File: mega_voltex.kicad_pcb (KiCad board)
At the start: 2 copper layers, 10 parts, among them J1 Arduino_Mega_Header

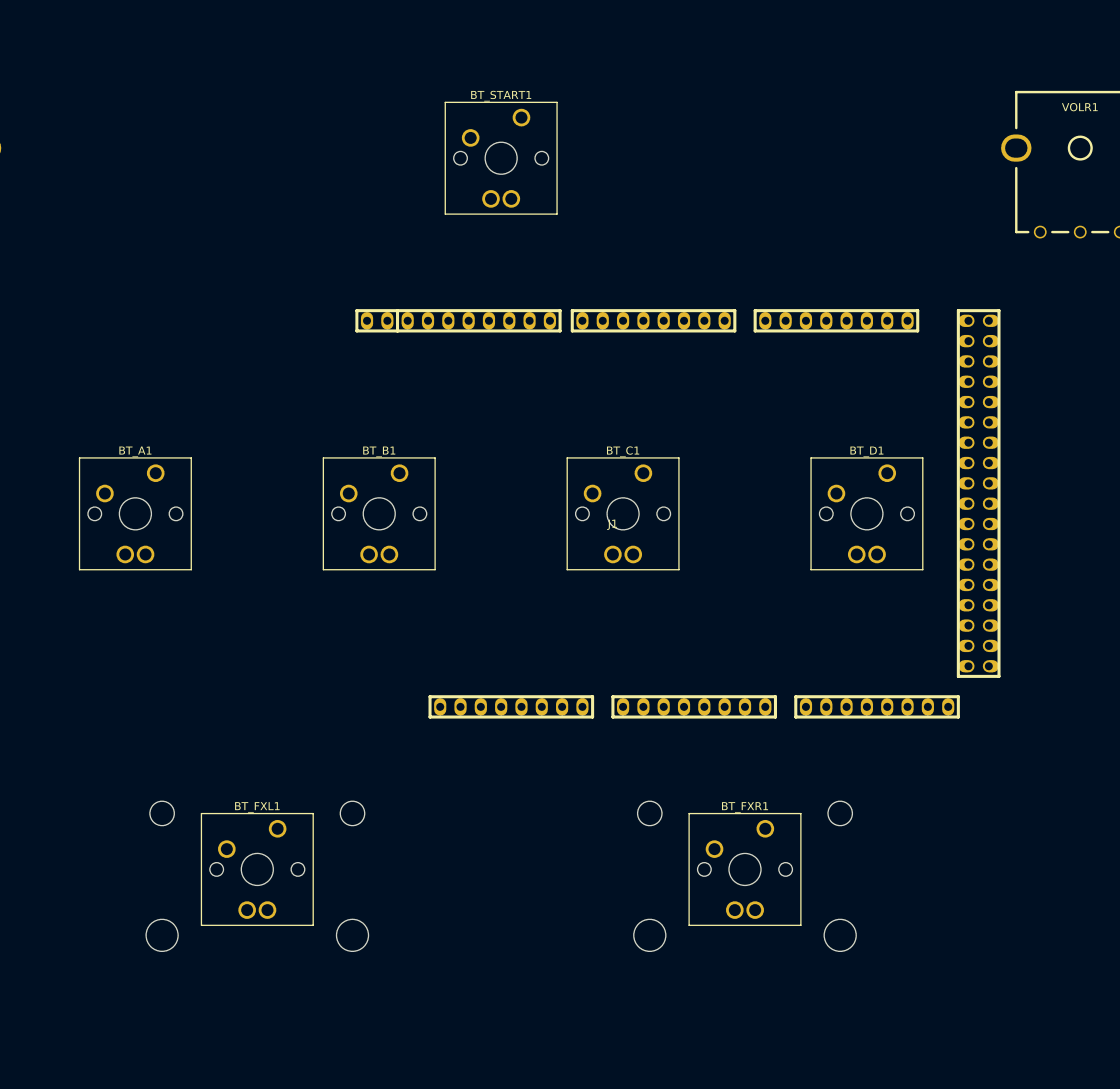
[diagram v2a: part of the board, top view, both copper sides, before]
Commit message: Added headers & resistors for LEDs
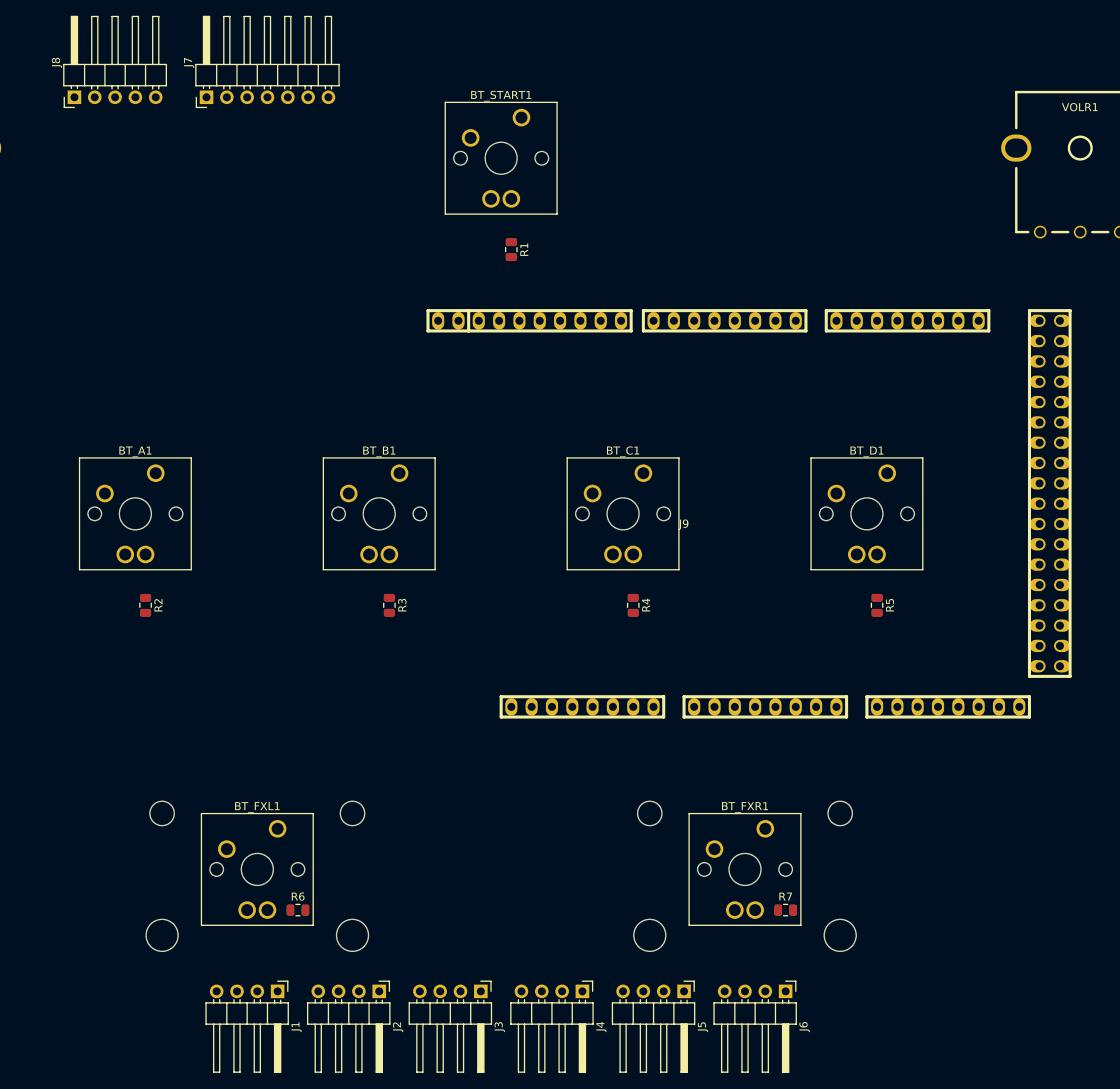
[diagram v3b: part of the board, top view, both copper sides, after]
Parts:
- added J2: HEADER_4, Connector_PinHeader_2.54mm:PinHeader_1x04_P2.54mm_Horizontal, F.Cu at (116.8, 142.2)
- added J3: HEADER_4, Connector_PinHeader_2.54mm:PinHeader_1x04_P2.54mm_Horizontal, F.Cu at (129.5, 142.2)
- added J4: HEADER_4, Connector_PinHeader_2.54mm:PinHeader_1x04_P2.54mm_Horizontal, F.Cu at (142.2, 142.2)
- added J5: HEADER_4, Connector_PinHeader_2.54mm:PinHeader_1x04_P2.54mm_Horizontal, F.Cu at (154.9, 142.2)
- added J6: HEADER_4, Connector_PinHeader_2.54mm:PinHeader_1x04_P2.54mm_Horizontal, F.Cu at (167.6, 142.2)
- added J7: HEADER_7, Connector_PinHeader_2.54mm:PinHeader_1x07_P2.54mm_Horizontal, F.Cu at (95.2, 30.5)
- added J8: HEADER_5, Connector_PinHeader_2.54mm:PinHeader_1x05_P2.54mm_Horizontal, F.Cu at (78.7, 30.5)
- added J9: Arduino_Mega_Header, mega_voltex:arduino_mega_header, F.Cu at (154.9, 82.5)
- added R1: R_Small_US, Resistor_SMD:R_0805_2012Metric, F.Cu at (133.3, 49.5)
- added R2: R_Small_US, Resistor_SMD:R_0805_2012Metric, F.Cu at (87.6, 94.0)
- added R3: R_Small_US, Resistor_SMD:R_0805_2012Metric, F.Cu at (118.1, 94.0)
- added R4: R_Small_US, Resistor_SMD:R_0805_2012Metric, F.Cu at (148.6, 94.0)
- added R5: R_Small_US, Resistor_SMD:R_0805_2012Metric, F.Cu at (179.1, 94.0)
- added R6: R_Small_US, Resistor_SMD:R_0805_2012Metric, F.Cu at (106.7, 132.1)
- added R7: R_Small_US, Resistor_SMD:R_0805_2012Metric, F.Cu at (167.6, 132.1)
- J1: value Arduino_Mega_Header -> HEADER_4; footprint mega_voltex:arduino_mega_header -> Connector_PinHeader_2.54mm:PinHeader_1x04_P2.54mm_Horizontal
- moved J1 72.9 mm to (104.1, 142.2), turned to 270 degrees
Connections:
- BT_A1 pad 4: LT_A -> Net-(BT_A1-Pad4)
- BT_B1 pad 4: LT_B -> Net-(BT_B1-Pad4)
- BT_C1 pad 4: LT_C -> Net-(BT_C1-Pad4)
- BT_D1 pad 4: LT_D -> Net-(BT_D1-Pad4)
- BT_FXL1 pad 4: LT_FXL -> Net-(BT_FXL1-Pad4)
- BT_FXR1 pad 4: LT_FXR -> Net-(BT_FXR1-Pad4)
- BT_START1 pad 4: LT_START -> Net-(BT_START1-Pad4)
- J1 pad 1: (no net) -> GND
- J1 pad 2: Net-(J1-Pad2) -> LED1_R
- J1 pad 3: Net-(J1-Pad3) -> LED1_G
- J1 pad 4: Net-(J1-Pad4) -> LED1_B
- VOLL1 pad A: Net-(VOLL1-PadA) -> VOLL_A
- VOLL1 pad C: Net-(VOLL1-PadC) -> VOLL_B
- VOLR1 pad A: Net-(VOLR1-PadA) -> VOLR_A
- VOLR1 pad C: Net-(VOLR1-PadC) -> VOLR_B

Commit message: Lots of changes. PCB without LED1-5 headers is nearly complete
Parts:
- removed J1, J2, J3, J4, J5, J6: HEADER_4, Connector_PinHeader_2.54mm:PinHeader_1x04_P2.54mm_Horizontal
- added D1: LED_RGB, LED_SMD:LED_RGB_Cree-PLCC-6_6x5mm_P2.1mm, F.Cu at (57.5, 25.0)
- added D2: LED_RGB, LED_SMD:LED_RGB_Cree-PLCC-6_6x5mm_P2.1mm, F.Cu at (122.5, 25.0)
- added D3: LED_RGB, LED_SMD:LED_RGB_Cree-PLCC-6_6x5mm_P2.1mm, F.Cu at (20.0, 85.0)
- added D4: LED_RGB, LED_SMD:LED_RGB_Cree-PLCC-6_6x5mm_P2.1mm, F.Cu at (160.0, 85.0)
- added Q1: PN2222A, Package_TO_SOT_SMD:SOT-323_SC-70, F.Cu at (154.5, 91.5)
- added Q2: PN2222A, Package_TO_SOT_SMD:SOT-323_SC-70, F.Cu at (154.5, 96.0)
- added Q3: PN2222A, Package_TO_SOT_SMD:SOT-323_SC-70, F.Cu at (154.5, 100.5)
- added R10: R_Small_US, Resistor_SMD:R_0805_2012Metric, F.Cu at (70.0, 28.5)
- added R11: R_Small_US, Resistor_SMD:R_0805_2012Metric, F.Cu at (135.0, 21.2)
- added R12: R_Small_US, Resistor_SMD:R_0805_2012Metric, F.Cu at (135.0, 25.0)
- added R13: R_Small_US, Resistor_SMD:R_0805_2012Metric, F.Cu at (135.0, 28.8)
- added R14: R_Small_US, Resistor_SMD:R_0805_2012Metric, F.Cu at (16.5, 75.0)
- added R15: R_Small_US, Resistor_SMD:R_0805_2012Metric, F.Cu at (20.0, 75.0)
- added R16: R_Small_US, Resistor_SMD:R_0805_2012Metric, F.Cu at (23.5, 75.0)
- added R17: R_Small_US, Resistor_SMD:R_0805_2012Metric, F.Cu at (156.5, 75.0)
- added R18: R_Small_US, Resistor_SMD:R_0805_2012Metric, F.Cu at (160.0, 75.0)
- added R19: R_Small_US, Resistor_SMD:R_0805_2012Metric, F.Cu at (163.5, 75.0)
- added R8: R_Small_US, Resistor_SMD:R_0805_2012Metric, F.Cu at (70.0, 21.5)
- added R9: R_Small_US, Resistor_SMD:R_0805_2012Metric, F.Cu at (70.0, 25.0)
- J7, J8, R1, R2, R3, R4, R5, R6, R7: moved to B.Cu
- moved J7 69.6 mm to (159.0, 58.5), turned to 0 degrees
- moved J9 52.9 mm to (105.0, 65.0)
- moved VOLR1 50.9 mm to (155.0, 25.0)
- moved BT_FXR1 48.2 mm to (120.0, 105.0)
- moved R7 48.0 mm to (125.1, 110.0)
- moved BT_FXL1 47.3 mm to (60.0, 105.0)
- moved R6 47.2 mm to (65.0, 110.0)
- moved BT_D1 47.0 mm to (135.0, 65.0)
- moved BT_C1 46.6 mm to (105.0, 65.0)
- moved BT_B1 46.1 mm to (75.0, 65.0)
- moved R5 45.8 mm to (140.0, 70.0), turned to 0 degrees
- moved BT_A1 45.6 mm to (45.0, 65.0)
- moved R4 45.4 mm to (110.1, 70.0), turned to 0 degrees
- moved BT_START1 45.3 mm to (90.0, 25.0)
- moved R3 45.0 mm to (80.1, 70.0), turned to 0 degrees
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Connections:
- J7 pad 1: K1_A -> K1_4
- J7 pad 2: K1_B -> K1_3
- J7 pad 3: K1_C -> K1_2
- J7 pad 5: K1_2 -> K1_C
- J7 pad 6: K1_3 -> K1_B
- J7 pad 7: K1_4 -> K1_A
- J8 pad 3: R1_TX -> R1_DET
- J8 pad 5: R1_DET -> R1_TX
- J9 pad 17: LED6_R -> Net-(J9-Pad17)
- J9 pad 18: LED6_G -> Net-(J9-Pad18)
- J9 pad 19: LED6_B -> Net-(J9-Pad19)
- J9 pad 57: K1_A -> K1_C
- J9 pad 59: K1_C -> K1_A
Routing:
- net LED6_R: track 0.00 -> 331.2 mm, vias 0 -> 6
- net LED6_G: track 0.00 -> 331.1 mm, vias 0 -> 6
- net LED6_B: track 0.00 -> 329.9 mm, vias 0 -> 4
- net 12V: track 0.00 -> 278.0 mm, vias 0 -> 4
- net VOLL_A: track 0.00 -> 152.3 mm, vias 0 -> 2
- net VOLL_B: track 0.00 -> 149.0 mm
- net LT_FXL: track 0.00 -> 118.9 mm
- net 5V: track 0.00 -> 117.6 mm, vias 0 -> 3
- net BT_START: track 0.00 -> 113.8 mm, vias 0 -> 2
- net LT_A: track 0.00 -> 104.7 mm
- net LT_START: track 0.00 -> 102.3 mm, vias 0 -> 1
- net BT_A: track 0.00 -> 77.0 mm
- net LT_B: track 0.00 -> 73.9 mm
- net LT_FXR: track 0.00 -> 62.3 mm
- net BT_FXL: track 0.00 -> 57.8 mm
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- added copper zone on F.Cu, net GND
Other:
- board outline added: 170 x 115 mm

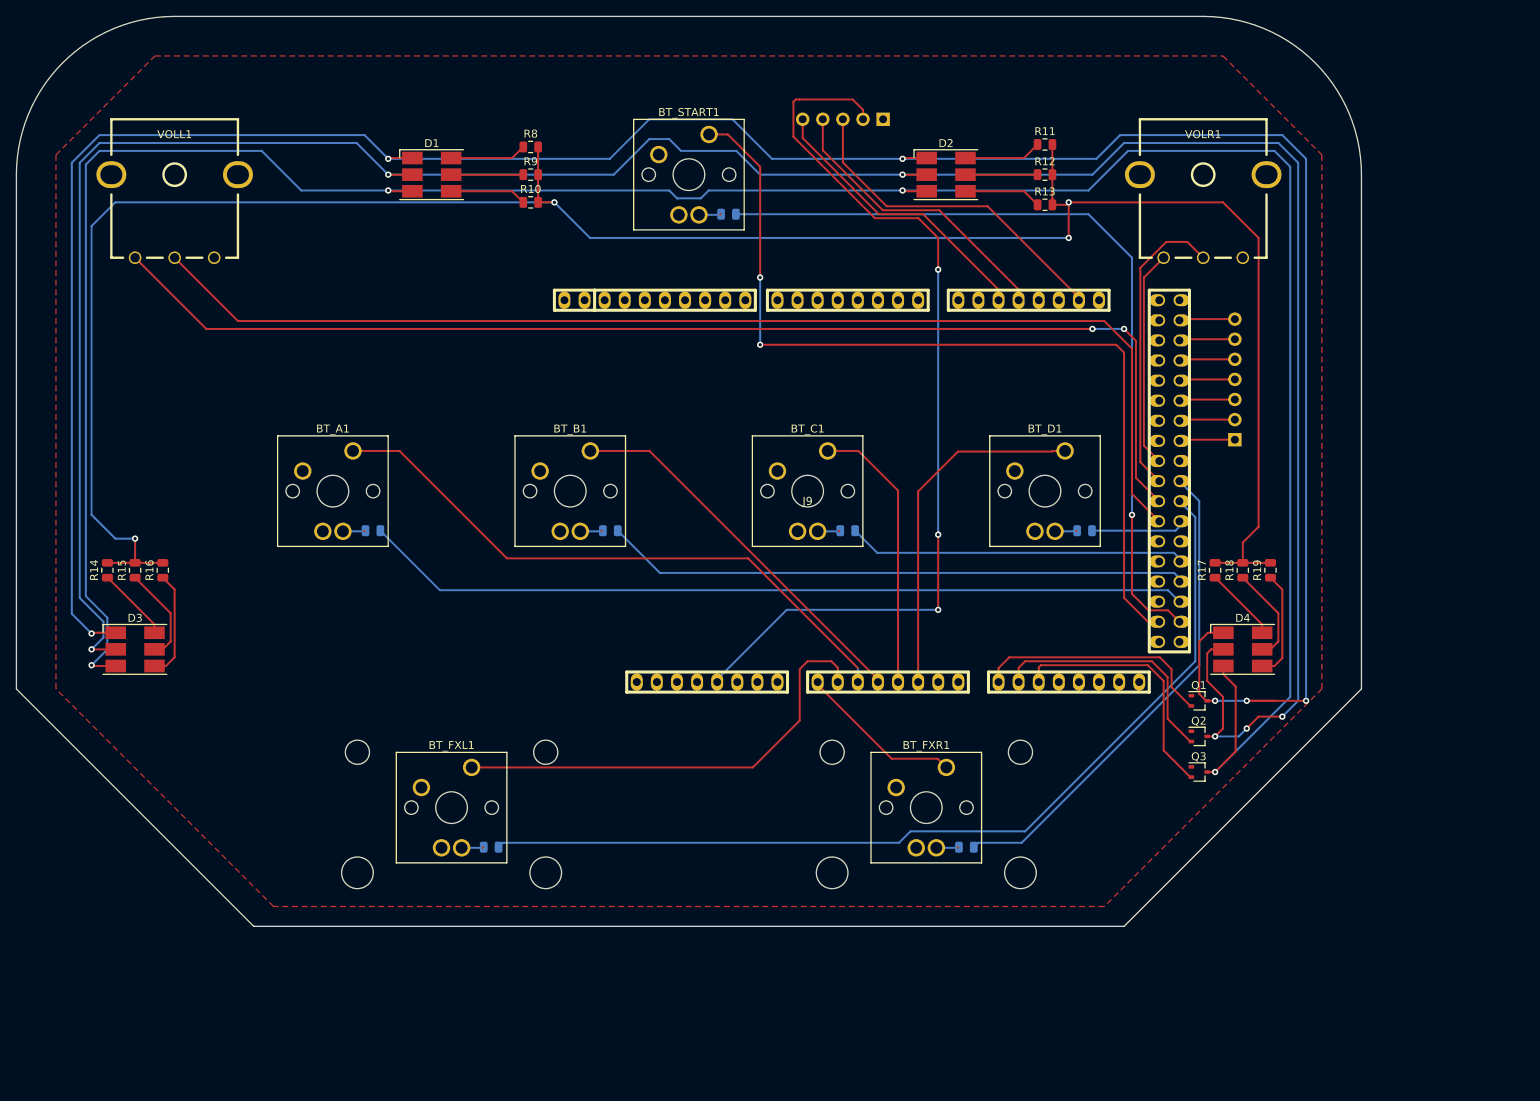
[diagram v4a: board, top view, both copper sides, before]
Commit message: Fixed some library/footprint difference issues with LEDs and transistors
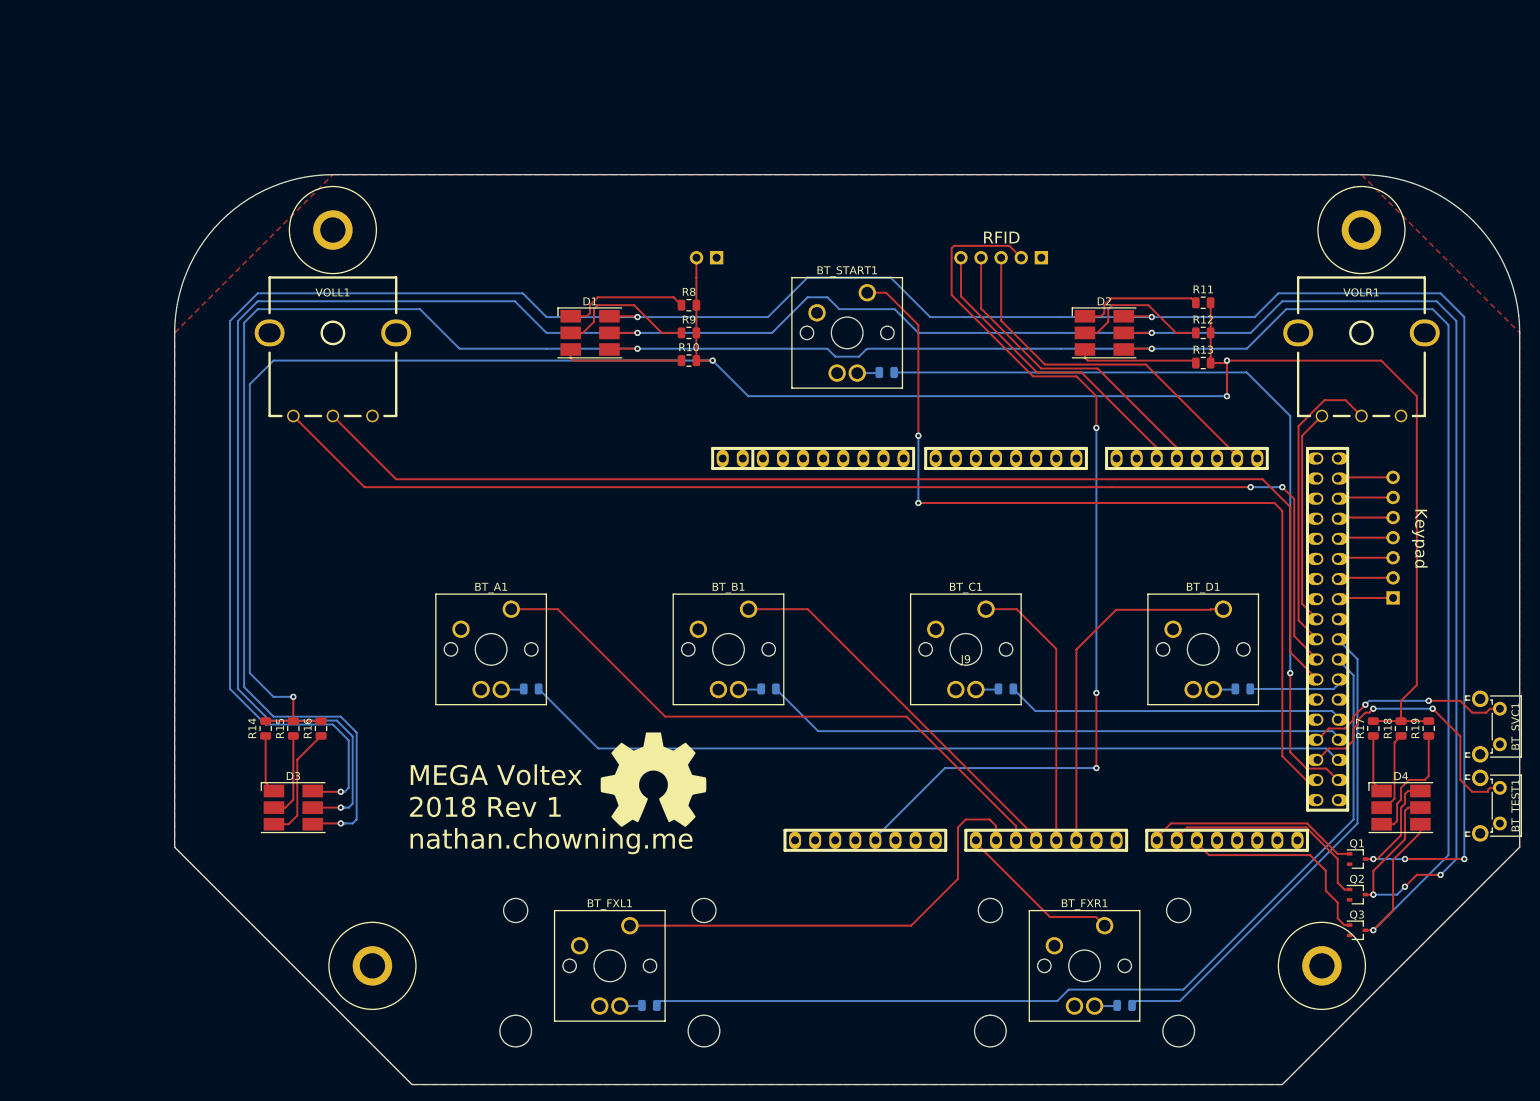
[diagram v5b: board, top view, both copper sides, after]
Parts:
- added BT_SVC1: SW_Push, Button_Switch_THT:SW_Tactile_SPST_Angled_PTS645Vx58-2LFS, F.Cu at (192.5, 92.5)
- added BT_TEST1: SW_Push, Button_Switch_THT:SW_Tactile_SPST_Angled_PTS645Vx58-2LFS, F.Cu at (192.5, 102.5)
- added J6: HEADER_2, Connector_PinHeader_2.54mm:PinHeader_1x02_P2.54mm_Horizontal, B.Cu at (93.5, 35.5)
- added Mounting Hole: Banana_Jack_1Pin, Connector:Banana_Jack_1Pin, F.Cu at (170.0, 125.0)
- added Mounting Hole: Banana_Jack_1Pin, Connector:Banana_Jack_1Pin, F.Cu at (50.0, 125.0)
- added Mounting Hole: Banana_Jack_1Pin, Connector:Banana_Jack_1Pin, F.Cu at (45.0, 32.0)
- added REF**: Banana_Jack_1Pin, Connector:Banana_Jack_1Pin, F.Cu at (175.0, 32.0)
- added REF**: OSHW-Symbol_13.4x12mm_SilkScreen, Symbol:OSHW-Symbol_13.4x12mm_SilkScreen, F.Cu at (85.5, 101.5)
- D1, D2, D3, D4: value LED_RGB -> RGBLED_CREE_CLP6C
- Q1, Q2, Q3: value PN2222A -> MMBT2222AWT1G
- moved BT_A1 28.3 mm to (65.0, 85.0)
- moved BT_B1 28.3 mm to (95.0, 85.0)
- moved BT_C1 28.3 mm to (125.0, 85.0)
- moved BT_D1 28.3 mm to (155.0, 85.0)
- moved BT_FXL1 28.3 mm to (80.0, 125.0)
- moved BT_FXR1 28.3 mm to (140.0, 125.0)
- moved BT_START1 28.3 mm to (110.0, 45.0)
- moved D1 28.3 mm to (77.5, 45.0)
- moved D2 28.3 mm to (142.5, 45.0)
- moved D3 28.3 mm to (40.0, 105.0)
- moved D4 28.3 mm to (180.0, 105.0)
- moved J7 28.3 mm to (179.0, 78.5)
- moved J9 28.3 mm to (125.0, 85.0)
- moved Q1 28.3 mm to (174.5, 111.5)
- moved Q2 28.3 mm to (174.5, 116.0)
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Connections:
- D1 pad 1: LED6_R -> Net-(D1-Pad1)
- D1 pad 2: LED6_G -> Net-(D1-Pad2)
- D1 pad 3: LED6_B -> Net-(D1-Pad3)
- D1 pad 4: Net-(D1-Pad4) -> LED6_B
- D1 pad 5: Net-(D1-Pad5) -> LED6_G
- D1 pad 6: Net-(D1-Pad6) -> LED6_R
- D2 pad 1: LED6_R -> Net-(D2-Pad1)
- D2 pad 2: LED6_G -> Net-(D2-Pad2)
- D2 pad 3: LED6_B -> Net-(D2-Pad3)
- D2 pad 4: Net-(D2-Pad4) -> LED6_B
- D2 pad 5: Net-(D2-Pad5) -> LED6_G
- D2 pad 6: Net-(D2-Pad6) -> LED6_R
- D3 pad 1: LED6_R -> Net-(D3-Pad1)
- D3 pad 2: LED6_G -> Net-(D3-Pad2)
- D3 pad 3: LED6_B -> Net-(D3-Pad3)
- D3 pad 4: Net-(D3-Pad4) -> LED6_B
- D3 pad 5: Net-(D3-Pad5) -> LED6_G
- D3 pad 6: Net-(D3-Pad6) -> LED6_R
- D4 pad 1: LED6_R -> Net-(D4-Pad1)
- D4 pad 2: LED6_G -> Net-(D4-Pad2)
- D4 pad 3: LED6_B -> Net-(D4-Pad3)
- D4 pad 4: Net-(D4-Pad4) -> LED6_B
- D4 pad 5: Net-(D4-Pad5) -> LED6_G
- D4 pad 6: Net-(D4-Pad6) -> LED6_R
- Q1 pad 1: GND -> Net-(J9-Pad17)
- Q1 pad 2: Net-(J9-Pad17) -> GND
- Q2 pad 1: GND -> Net-(J9-Pad18)
- Q2 pad 2: Net-(J9-Pad18) -> GND
- Q3 pad 1: GND -> Net-(J9-Pad19)
- Q3 pad 2: Net-(J9-Pad19) -> GND
- R10 pad 1: Net-(D1-Pad4) -> Net-(D1-Pad3)
- R11 pad 1: Net-(D2-Pad6) -> Net-(D2-Pad1)
- R12 pad 1: Net-(D2-Pad5) -> Net-(D2-Pad2)
- R13 pad 1: Net-(D2-Pad4) -> Net-(D2-Pad3)
- R14 pad 1: Net-(D3-Pad6) -> Net-(D3-Pad1)
- R15 pad 1: Net-(D3-Pad5) -> Net-(D3-Pad2)
- R16 pad 1: Net-(D3-Pad4) -> Net-(D3-Pad3)
- R17 pad 1: Net-(D4-Pad6) -> Net-(D4-Pad1)
- R18 pad 1: Net-(D4-Pad5) -> Net-(D4-Pad2)
- R19 pad 1: Net-(D4-Pad4) -> Net-(D4-Pad3)
- R8 pad 1: Net-(D1-Pad6) -> Net-(D1-Pad1)
- R9 pad 1: Net-(D1-Pad5) -> Net-(D1-Pad2)
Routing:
- net BT_TEST: track 0.00 -> 34.8 mm, vias 0 -> 2
- net BT_SVC: track 0.00 -> 26.2 mm, vias 0 -> 2
- net Net-(D1-Pad2): track 0.00 -> 17.8 mm
- net Net-(D2-Pad2): track 0.00 -> 17.8 mm
- net Net-(D1-Pad1): track 0.00 -> 16.0 mm
- net Net-(D2-Pad1): track 0.00 -> 15.8 mm
- net Net-(D4-Pad3): track 0.00 -> 15.7 mm
- net Net-(D2-Pad3): track 0.00 -> 15.3 mm
- net Net-(D1-Pad3): track 0.00 -> 15.2 mm
- net Net-(D3-Pad3): track 0.00 -> 14.7 mm
- net LED6_B: track 329.9 -> 343.8 mm
- net Net-(D4-Pad4): track 13.7 -> 0.00 mm
- net LED6_G: track 331.1 -> 344.8 mm
- net Net-(D3-Pad4): track 13.7 -> 0.00 mm
- net LED6_R: track 331.2 -> 344.5 mm
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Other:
- board text added: "Keypad"
- board text added: "LED Power"
- board text added: "MEGA Voltex 2018 Rev 1 nathan.chowning.me"
- board text added: "RFID"
